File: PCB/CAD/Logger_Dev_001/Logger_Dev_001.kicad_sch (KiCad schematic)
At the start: 1 part, among them U2 ESP32-C6-WROOM-1

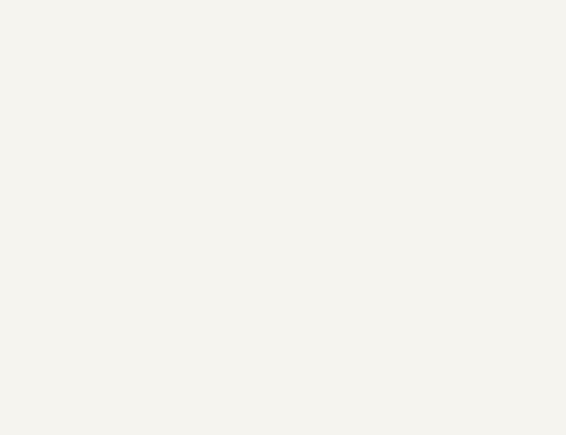
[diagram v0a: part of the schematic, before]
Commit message: Main Component Selection
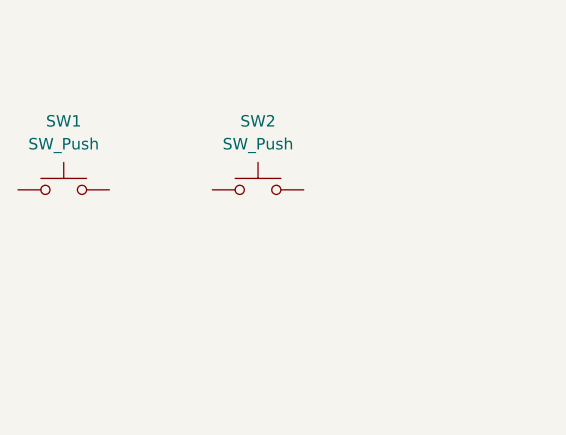
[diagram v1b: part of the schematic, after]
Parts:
- added SW1, SW2: SW_Push, symbol Switch:SW_Push
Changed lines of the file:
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@@
 	(paper "A4")
+	(symbol
+		(lib_id "Switch:SW_Push")
+		(at 62.23 80.01 0)
+		(unit 1)
+		(exclude_from_sim no)
+		(in_bom yes)
+		(on_board yes)
+		(dnp no)
+		(fields_autoplaced yes)
+		(property "Reference" "SW1"
+			(at 62.23 72.39 0)
+			(effects
+				(font
+					(size 1.27 1.27)
+				)
+			)
+		)
+		(property "Value" "SW_Push"
+			(at 62.23 74.93 0)
+			(effects
+				(font
+					(size 1.27 1.27)
+				)
+			)
+		)
+		(property "Footprint" ""
+			(at 62.23 74.93 0)
+			(effects
+				(font
+					(size 1.27 1.27)
+				)
+				(hide yes)
+			)
+		)
+		(property "Datasheet" "~"
+			(at 62.23 74.93 0)
+			(effects
+				(font
+					(size 1.27 1.27)
+				)
+				(hide yes)
+			)
+		)
+		(property "Description" "Push button switch, generic, two pins"
+			(at 62.23 80.01 0)
+			(effects
+				(font
+					(size 1.27 1.27)
+				)
+				(hide yes)
+			)
+		)
+		(pin "2"
+		)
+		(pin "1"
+		)
+		(instances
+			(project ""
+				(path "/9546b831-c7ee-4f40-8993-5fd5a38d4078"
+					(reference "SW1")
+					(unit 1)
+				)
+			)
+		)
+	)
 	(symbol
 		(lib_id "Espressif:ESP32-C6-WROOM-1")
@@
 					(unit 1)
 				)
+			)
+		)
+	)
+	(symbol
+		(lib_id "Switch:SW_Push")
+		(at 83.82 80.01 0)
+		(unit 1)
+		(exclude_from_sim no)
+		(in_bom yes)
+		(on_board yes)
+		(dnp no)
+		(fields_autoplaced yes)
+		(property "Reference" "SW2"
+			(at 83.82 72.39 0)
+			(effects
+				(font
+					(size 1.27 1.27)
+				)
+			)
+		)
+		(property "Value" "SW_Push"
+			(at 83.82 74.93 0)
+			(effects
+				(font
+					(size 1.27 1.27)
+				)
+			)
+		)
+		(property "Footprint" ""
+			(at 83.82 74.93 0)
+			(effects
+				(font
+					(size 1.27 1.27)
+				)
+				(hide yes)
+			)
+		)
+		(property "Datasheet" "~"
+			(at 83.82 74.93 0)
+			(effects
+				(font
+					(size 1.27 1.27)
+				)
+				(hide yes)
+			)
+		)
+		(property "Description" "Push button switch, generic, two pins"
+			(at 83.82 80.01 0)
+			(effects
+				(font
+					(size 1.27 1.27)
+				)
+				(hide yes)
+			)
+		)
+		(pin "2"
+		)
+		(pin "1"
+		)
+		(instances
+			(project "Logger_Dev_001"
+				(path "/9546b831-c7ee-4f40-8993-5fd5a38d4078"
+					(reference "SW2")
+					(unit 1)
+				)

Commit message: Further Schematic update
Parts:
- added J1: Micro_SD_Card_Det2, symbol Connector:Micro_SD_Card_Det2
- added U1: NCP1117-5.0_SOT223, Package_TO_SOT_SMD:SOT-223-3_TabPin2, symbol Regulator_Linear:NCP1117-5.0_SOT223
- added U3: MCP7940N-xMNY, Package_DFN_QFN:DFN-8-1EP_3x2mm_P0.5mm_EP1.36x1.46mm, symbol Timer_RTC:MCP7940N-xMNY
- added U4: MCP2221AxSL, Package_SO:SOIC-14_3.9x8.7mm_P1.27mm, symbol Interface_USB:MCP2221AxSL
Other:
- moved on the sheet: SW1, SW2, U2

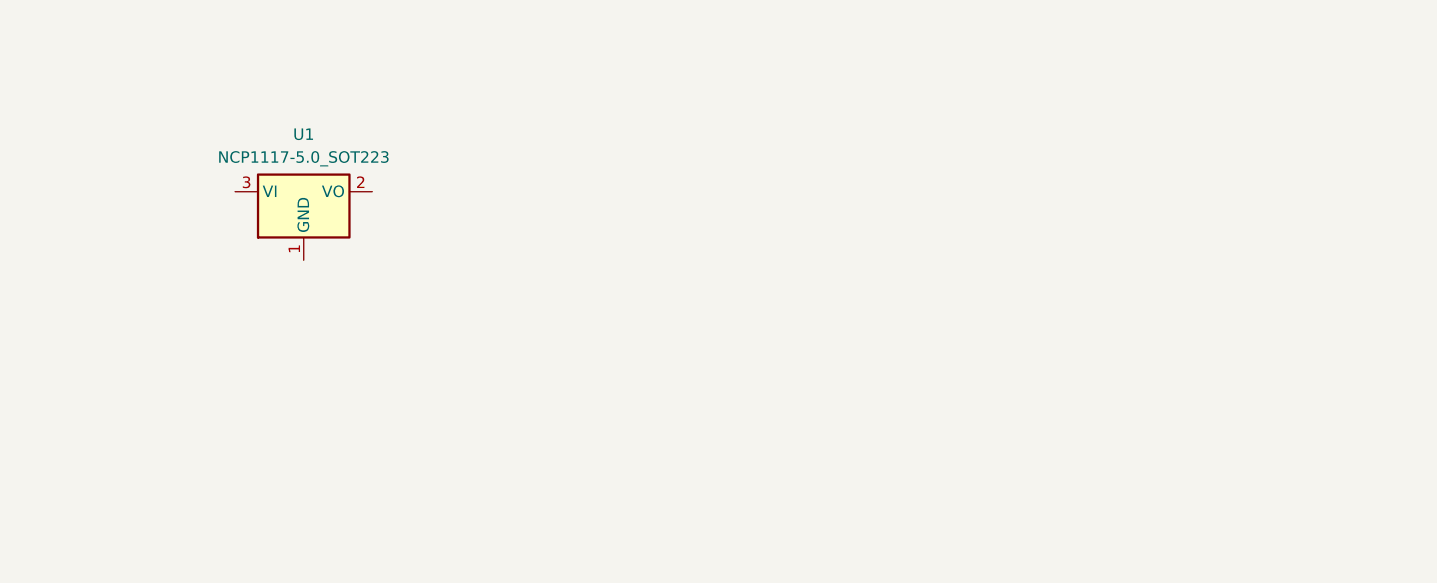
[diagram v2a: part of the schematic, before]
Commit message: Update to schematic
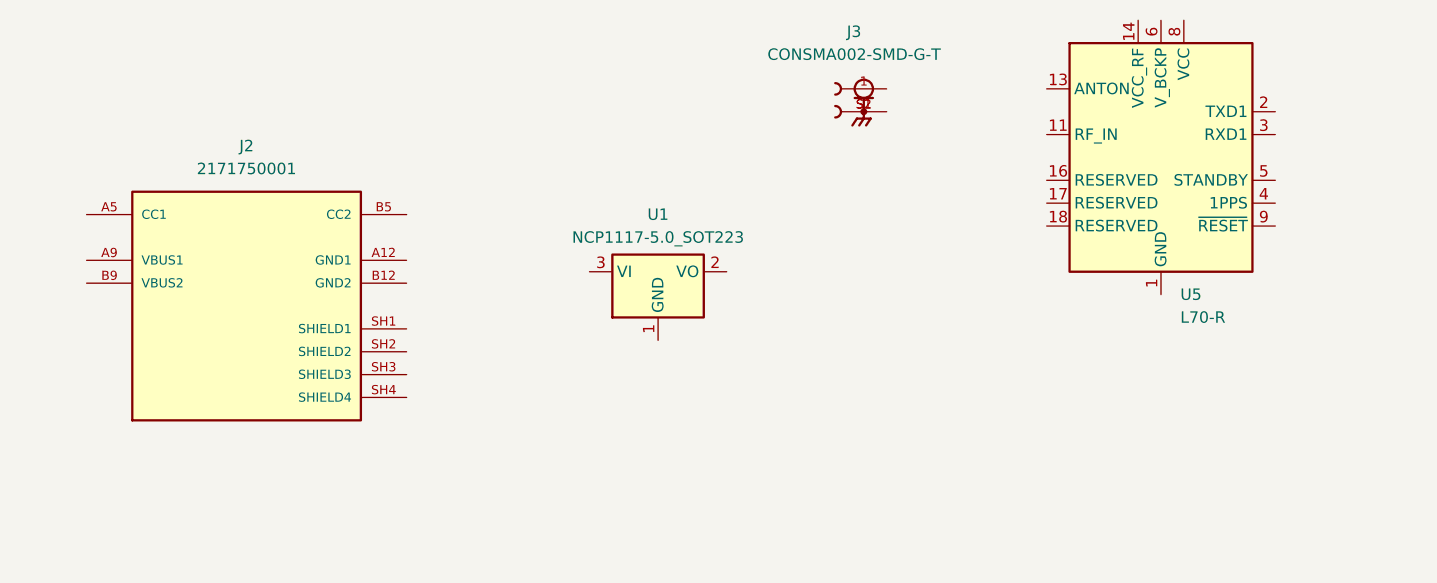
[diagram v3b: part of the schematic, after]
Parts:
- added J2: 2171750001, 2171750001:MOLEX_2171750001, symbol 2171750001:2171750001
- added J3: CONSMA002-SMD-G-T, CONSMA002-SMD-G-T:LINX_CONSMA002-SMD-G-T, symbol CONSMA002-SMD-G-T:CONSMA002-SMD-G-T
- added U5: L70-R, RF_GPS:Quectel_L70-R, symbol RF_GPS:L70-R
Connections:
- new net: U5.1 (GND), U5.10 (GND), U5.12 (GND)
- new net: J3.S1, J3.S2
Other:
- moved on the sheet: U1

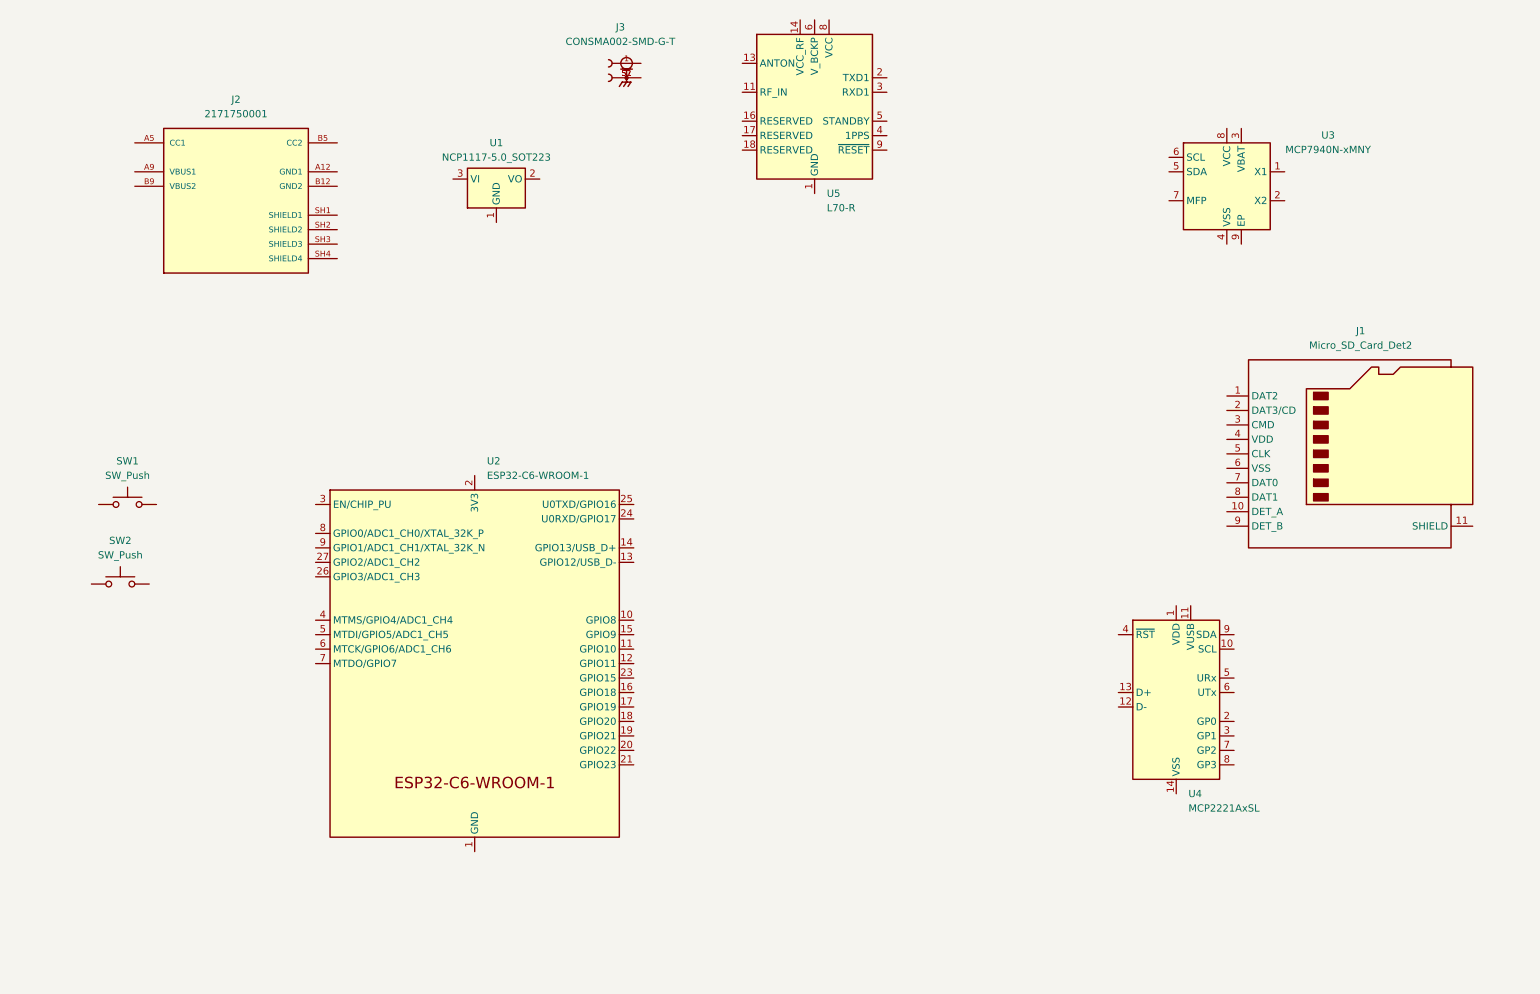
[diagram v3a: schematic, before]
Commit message: Hierarchy Sheets
Modules for each section:
-USB C Power Input to 3v3
-RTC Module
-GPS Module
-SD Storage Module
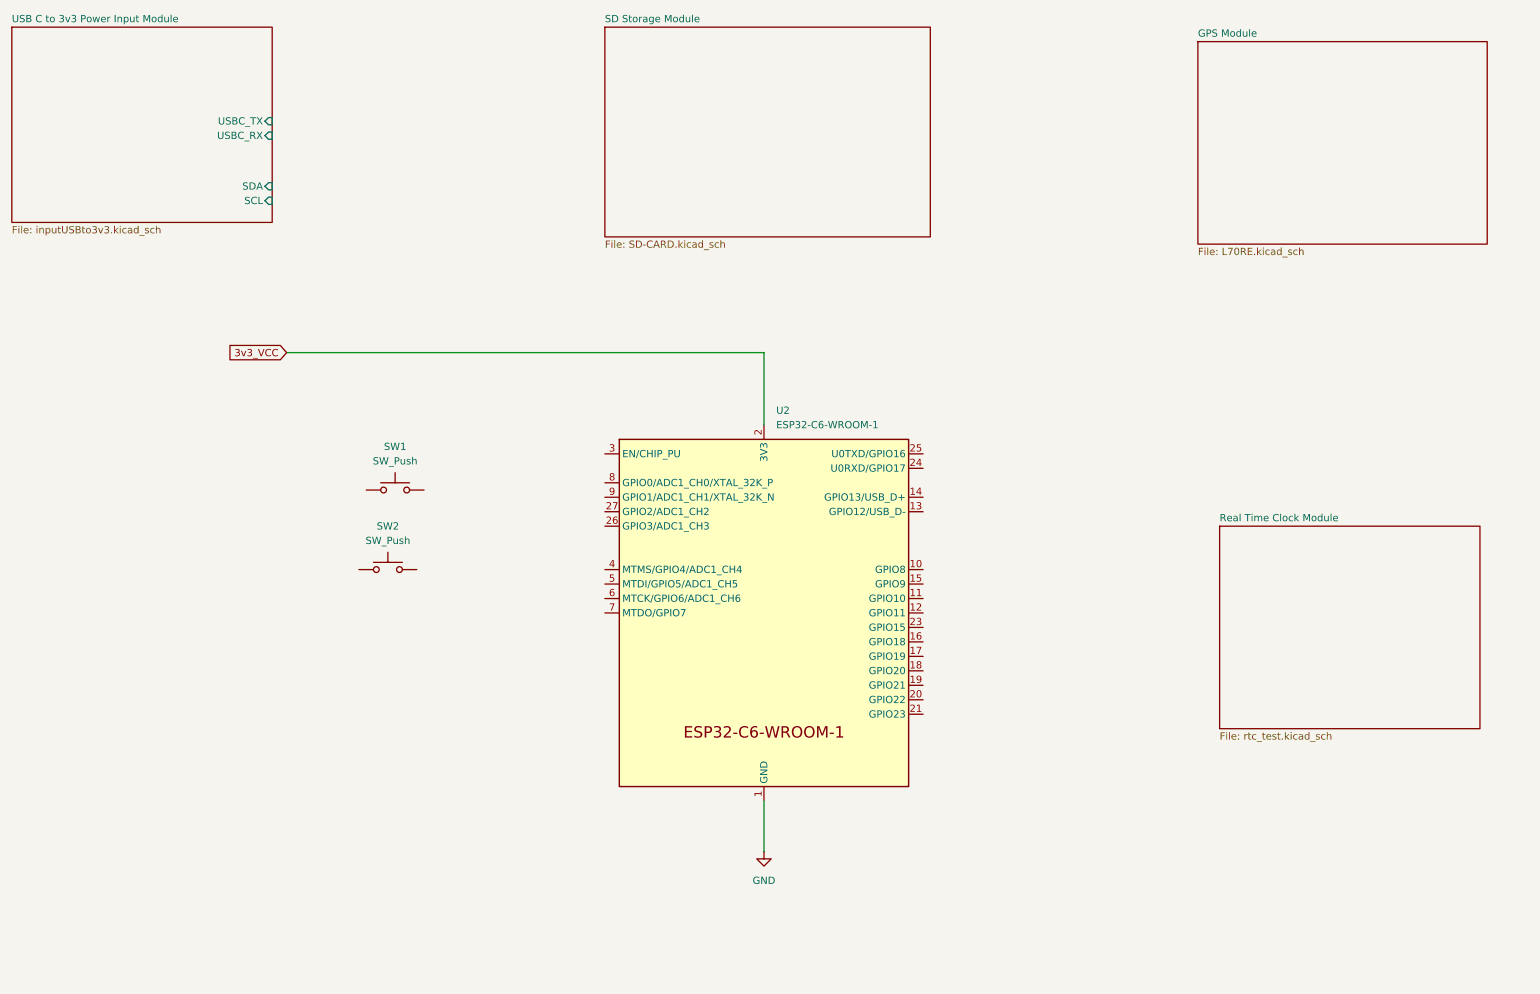
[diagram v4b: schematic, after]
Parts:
- removed J1: Micro_SD_Card_Det2, symbol Connector:Micro_SD_Card_Det2
- removed J2: 2171750001, 2171750001:MOLEX_2171750001, symbol 2171750001:2171750001
- removed J3: CONSMA002-SMD-G-T, CONSMA002-SMD-G-T:LINX_CONSMA002-SMD-G-T, symbol CONSMA002-SMD-G-T:CONSMA002-SMD-G-T
- removed U1: NCP1117-5.0_SOT223, Package_TO_SOT_SMD:SOT-223-3_TabPin2, symbol Regulator_Linear:NCP1117-5.0_SOT223
- removed U3: MCP7940N-xMNY, Package_DFN_QFN:DFN-8-1EP_3x2mm_P0.5mm_EP1.36x1.46mm, symbol Timer_RTC:MCP7940N-xMNY
- removed U4: MCP2221AxSL, Package_SO:SOIC-14_3.9x8.7mm_P1.27mm, symbol Interface_USB:MCP2221AxSL
- removed U5: L70-R, RF_GPS:Quectel_L70-R, symbol RF_GPS:L70-R
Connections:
- net GND: now reaches U2.1 (GND), U2.28 (GND), U2.29 (GND)
- net 3v3_VCC: now reaches U2.2 (3V3)
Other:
- added sheet GPS Module (L70RE.kicad_sch)
- added sheet Real Time Clock Module (rtc_test.kicad_sch)
- added sheet SD Storage Module (SD-CARD.kicad_sch)
- added sheet USB C to 3v3 Power Input Module (inputUSBto3v3.kicad_sch)
- moved on the sheet: SW1, SW2, U2

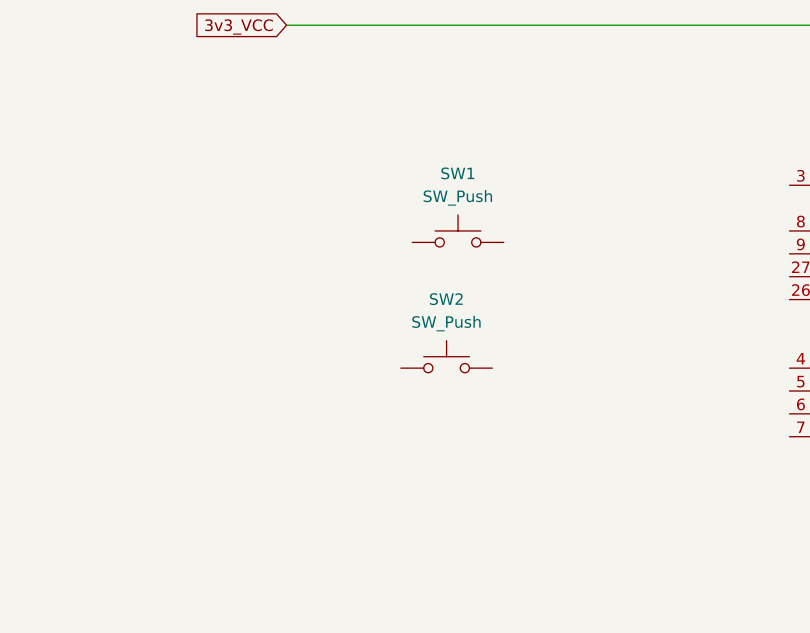
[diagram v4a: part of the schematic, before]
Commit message: JLCPCB Component Updates
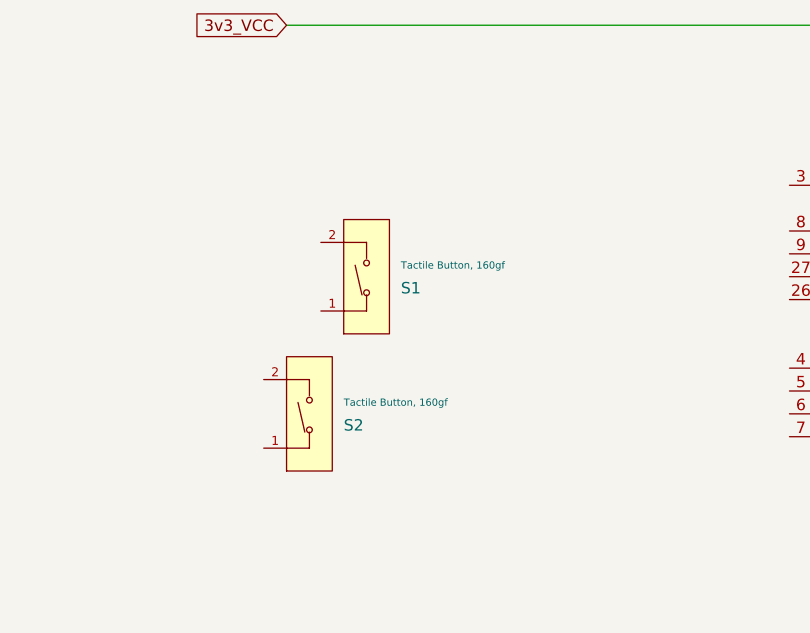
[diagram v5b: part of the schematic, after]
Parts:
- removed SW1, SW2: SW_Push, symbol Switch:SW_Push
- added S1, S2: Tactile Button, 160gf, PCM_JLCPCB:SW_TS-1088-AR02016, symbol PCM_JLCPCB-Connectors_Buttons:Tactile Button, 160gf, 12V, 50mA, 4.0mm

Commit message: Library Submodule Update
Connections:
- net SDIO_CMD: now reaches U2.16 (GPIO18)
- net SDIO_CLK: now reaches U2.17 (GPIO19)
- net SDIO_DATA0: now reaches U2.18 (GPIO20)
- net SDIO_DATA1: now reaches U2.19 (GPIO21)
- net SDIO_DATA2: now reaches U2.20 (GPIO22)
- net SDIO_DATA3: now reaches U2.21 (GPIO23)
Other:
- sheet SD Storage Module ports: added SDIO_CLK_SDCARD, SDIO_CMD_SDCARD, SDIO_DATA0_SDCARD, SDIO_DATA1_SDCARD, SDIO_DATA2_SDCARD, SDIO_DATA3_SDCARD; removed none
